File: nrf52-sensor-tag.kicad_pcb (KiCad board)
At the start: 2 copper layers, 36 x 36 mm, 22 parts, among them IC1 ISP1807-LR-RS, IC2 VEML6030, IC3 MS860702BA01-50, J3 Conn_01x07_Male

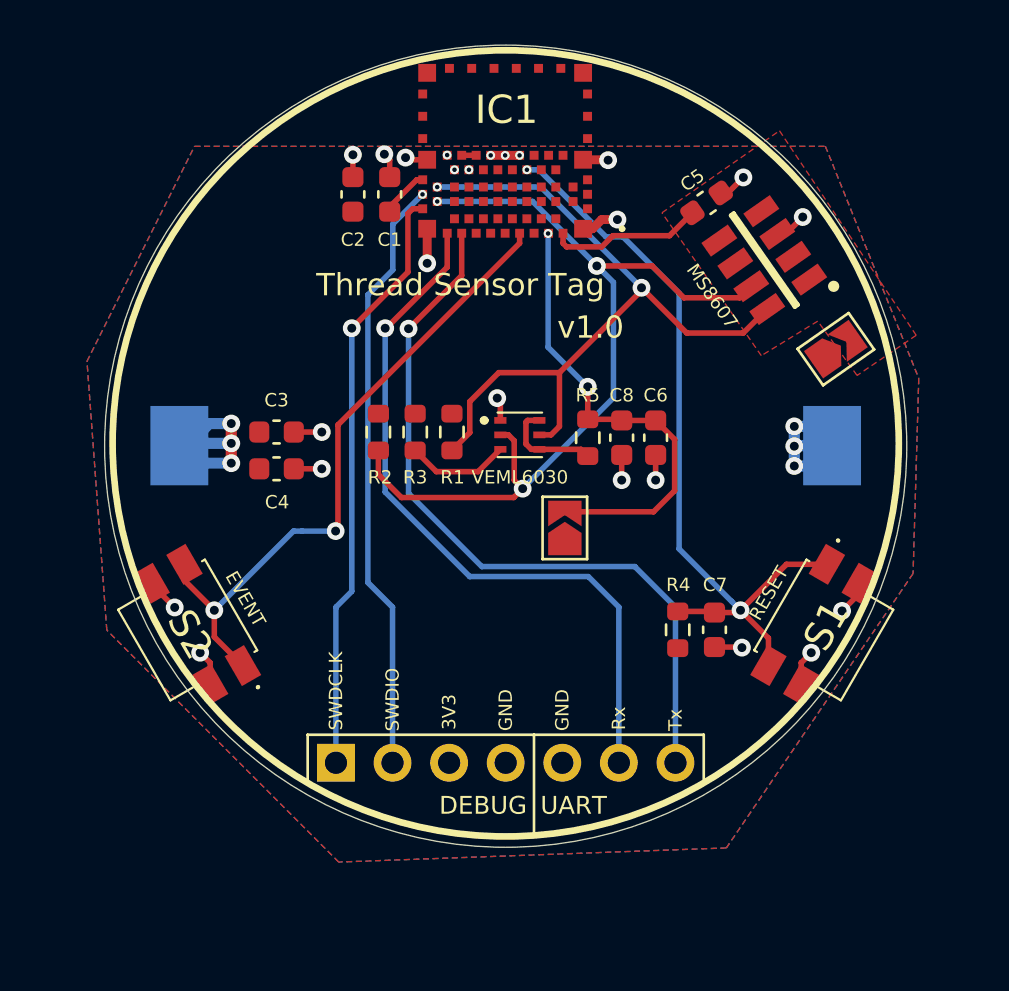
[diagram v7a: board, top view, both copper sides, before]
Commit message: Add MS88SF2 nRF52 Module and re-arranged components
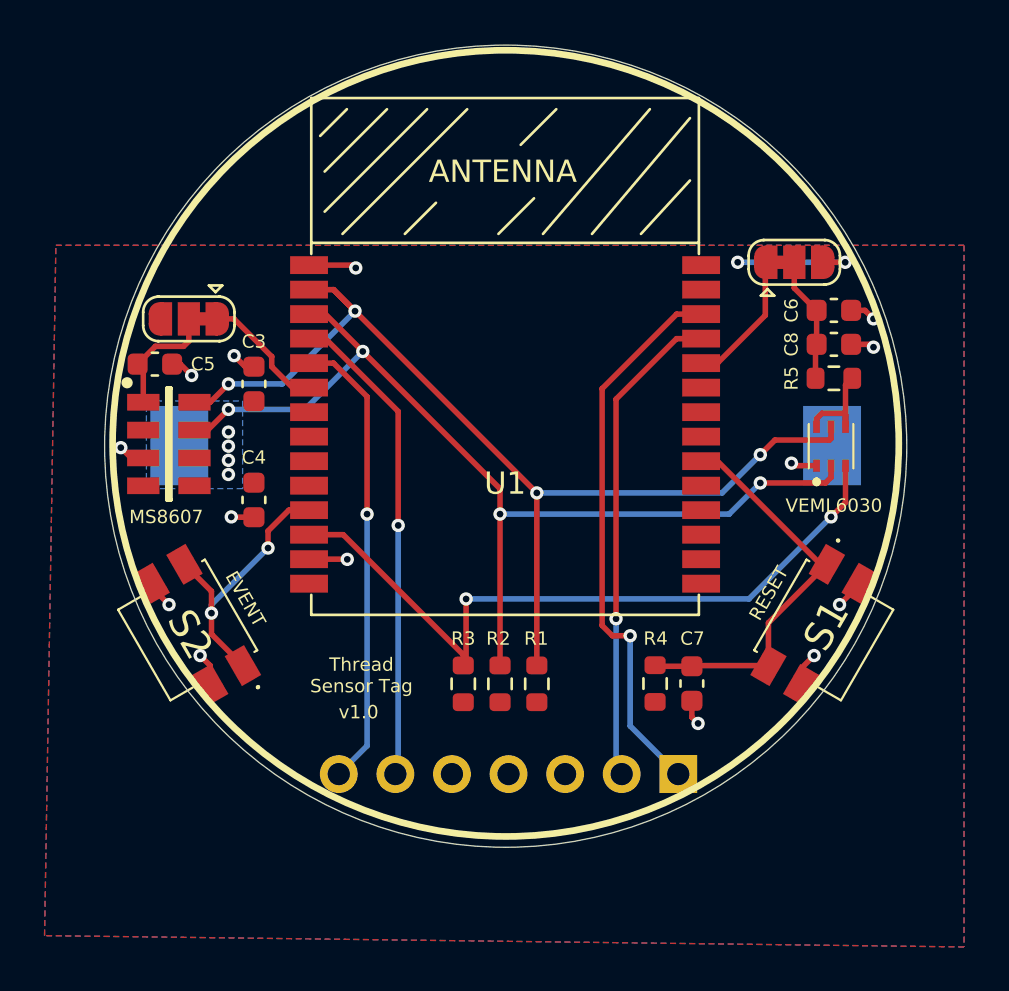
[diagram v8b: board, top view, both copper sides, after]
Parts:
- removed C1: 10uF, Capacitor_SMD:C_0603_1608Metric
- removed C2: 0.1uF, Capacitor_SMD:C_0603_1608Metric
- removed IC1: ISP1807-LR-RS, ISP1807:ISP1807LRRS
- added U1: MS88SF2, MS88SF2:MS88SF2, F.Cu at (121.3, 66.7)
- J3: moved to B.Cu
- JP1, JP2: value Jumper_NC_Small -> SolderJumper_3_Bridged12; footprint Jumper:SolderJumper-2_P1.3mm_Open_TrianglePad1.0x1.5mm -> Jumper:SolderJumper-3_P1.3mm_Bridged12_RoundedPad1.0x1.5mm
- moved IC3 28.0 mm to (106.6, 64.5), turned to 0 degrees
- moved C5 25.8 mm to (106.0, 61.0), turned to 0 degrees
- moved JP1 19.3 mm to (107.5, 58.9), turned to 180 degrees
- moved J3 15.4 mm to (129.5, 79.4)
- moved IC2 14.0 mm to (136.4, 64.6), turned to 90 degrees
- moved R2 12.6 mm to (121.5, 75.3), turned to 90 degrees
- moved R1 11.9 mm to (123.2, 75.3), turned to 90 degrees
- moved R3 11.5 mm to (119.9, 75.3), turned to 90 degrees
- moved R5 11.4 mm to (136.5, 61.6), turned to 0 degrees
- moved C8 10.4 mm to (136.5, 60.1), turned to 0 degrees
- moved C6 9.83 mm to (136.5, 58.5), turned to 0 degrees
- moved JP2 4.32 mm to (134.7, 56.4), turned to 0 degrees
- moved R4 2.62 mm to (128.5, 75.3)
- moved C7 2.62 mm to (130.1, 75.3)
- moved C3 2.39 mm to (110.5, 61.8), turned to 90 degrees
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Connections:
- C5 pad 1: /SENS1_VCC -> Net-(C5-Pad1)
- C6 pad 1: /SENS2_VCC -> Net-(C6-Pad1)
- C8 pad 1: /SENS2_VCC -> Net-(C6-Pad1)
- IC3 pad 1: /SENS1_VCC -> Net-(C5-Pad1)
- JP1 pad 1: /VCC -> /SENS1_VCC
- JP1 pad 2: /SENS2_VCC -> Net-(C5-Pad1)
- JP2 pad 1: /VCC -> /SENS2_VCC
- JP2 pad 2: /SENS1_VCC -> Net-(C6-Pad1)
- R5 pad 1: /SENS2_VCC -> Net-(C6-Pad1)
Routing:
- net /INT1: track 4.63 -> 33.2 mm, vias 0 -> 2
- net /BTN: track 29.6 -> 12.6 mm
- net /RESET: track 35.1 -> 18.3 mm, vias 2 -> 0
- net GND: track 34.2 -> 18.4 mm, vias 27 -> 14
- net /SENS2_VCC: track 21.0 -> 6.15 mm, vias 2 -> 0
- net /Tx: track 33.7 -> 20.7 mm
- net /SCL: track 33.9 -> 46.8 mm, vias 2 -> 4
- net /Rx: track 32.4 -> 21.7 mm
- net Net-(C6-Pad1): track 0.00 -> 5.64 mm
- net Net-(C5-Pad1): track 0.00 -> 5.54 mm
- net /SDA: track 39.3 -> 44.8 mm, vias 3 -> 4
- net /SWDIO: track 27.0 -> 21.9 mm
- net /VCC: track 10.7 -> 5.81 mm, vias 3 -> 6
- net /SWDCLK: track 26.7 -> 25.0 mm
- net /SENS1_VCC: track 6.96 -> 5.64 mm
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- added copper zone on B.Cu, net /VCC
- removed copper zone on F.Cu, net /SENS1_VCC
